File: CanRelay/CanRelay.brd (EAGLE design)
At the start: 93 x 65.5 mm, 22 parts

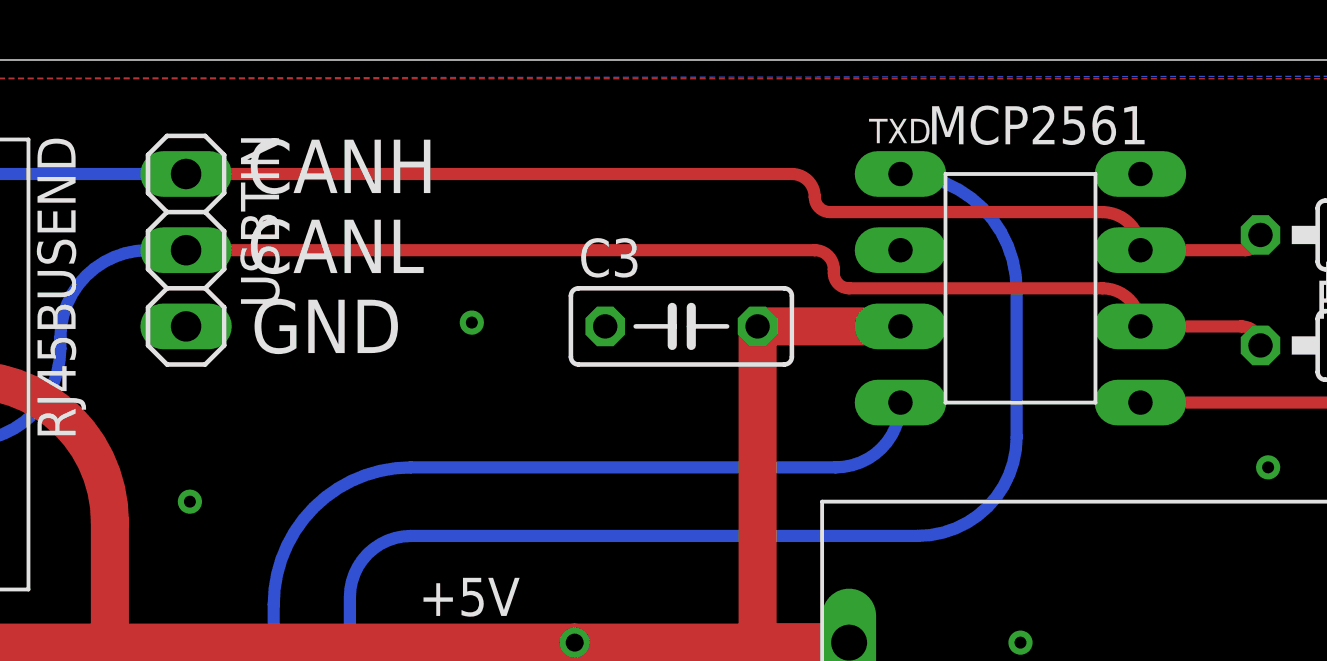
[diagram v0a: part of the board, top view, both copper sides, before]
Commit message: final tweaks on CanRelay - moving CANH and CANL lines around transceiver as opposed to among its pads. Moved therefore 5V for transceiver to bottom layer. final tweaks of isolation of both ground planes
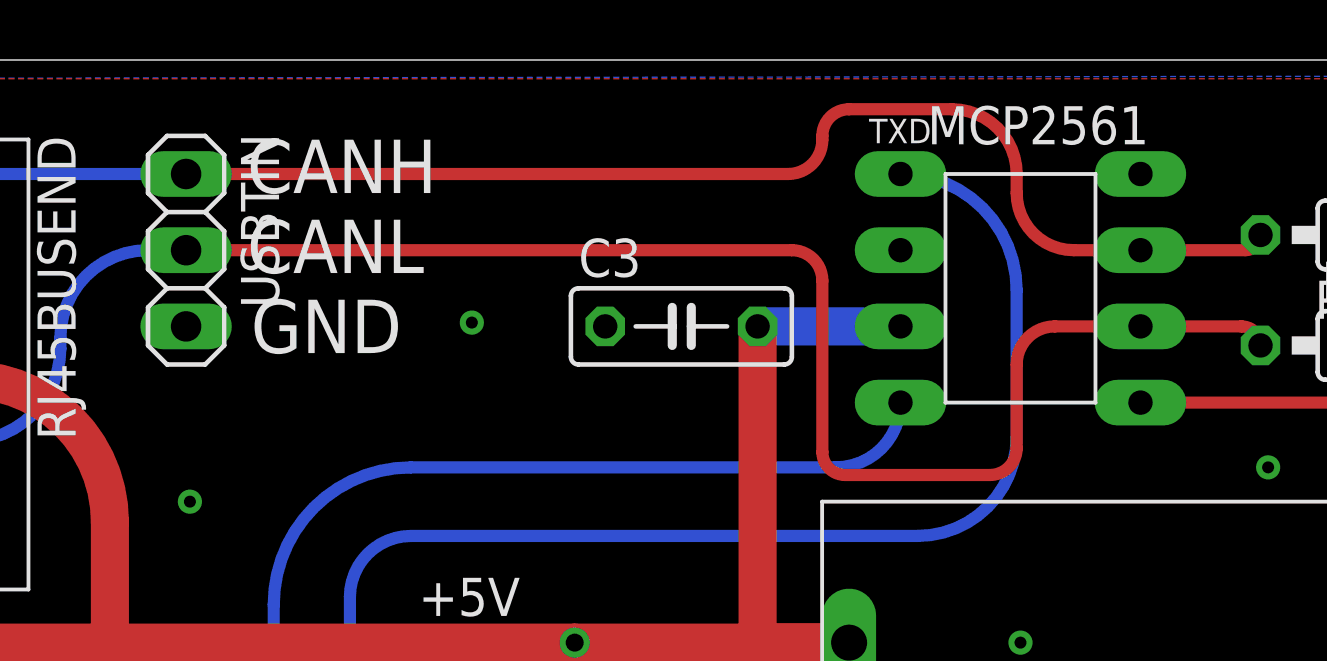
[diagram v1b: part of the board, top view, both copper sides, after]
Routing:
- net CANL: track 47.3 -> 56.3 mm
- net CANH: track 58.8 -> 61.0 mm
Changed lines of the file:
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@@
 <wire x1="13.808" y1="58.942" x2="13.808" y2="56.902" width="1.27" layer="1"/>
 <wire x1="13.808" y1="56.902" x2="13.808" y2="54.862" width="1.27" layer="1"/>
-<wire x1="44.895" y1="56.642" x2="40.132" y2="56.642" width="1.27" layer="1"/>
 <wire x1="5.461" y1="32.385" x2="8.763" y2="35.687" width="1.27" layer="1" curve="90"/>
 <wire x1="8.763" y1="35.687" x2="8.763" y2="42.672" width="1.27" layer="1"/>
@@
 <wire x1="34.163" y1="35.941" x2="34.036" y2="46.101" width="1.27" layer="16" curve="1.43232"/>
 <via x="34.036" y="46.101" extent="1-16" drill="0.6"/>
+<wire x1="40.132" y1="56.642" x2="44.895" y2="56.642" width="1.27" layer="16"/>
 </signal>
 <signal name="GND">
@@
 <contactref element="PWR" pad="GND1"/>
 <contactref element="PWR" pad="GND2"/>
-<polygon width="0.4064" layer="1" isolate="1">
+<polygon width="0.4064" layer="1" isolate="0.89">
 <vertex x="0.762" y="64.897"/>
 <vertex x="92.5" y="64.897"/>
@@
 </polygon>
 <contactref element="USBTIN" pad="3"/>
-<polygon width="0.4064" layer="16" isolate="1">
+<polygon width="0.4064" layer="16" isolate="0.6">
 <vertex x="0.762" y="64.897"/>
 <vertex x="92.5" y="65.024"/>
@@
 <wire x1="56.388" y1="59.182" x2="52.895" y2="59.182" width="0.4064" layer="1"/>
 <contactref element="USBTIN" pad="1"/>
-<wire x1="21.082" y1="61.722" x2="41.275" y2="61.722" width="0.4064" layer="1"/>
-<wire x1="52.895" y1="59.182" x2="51.625" y2="60.452" width="0.4064" layer="1" curve="90"/>
-<wire x1="51.625" y1="60.452" x2="42.545" y2="60.452" width="0.4064" layer="1"/>
-<wire x1="42.545" y1="60.452" x2="42.037" y2="60.96" width="0.4064" layer="1" curve="-90"/>
-<wire x1="42.037" y1="60.96" x2="41.275" y2="61.722" width="0.4064" layer="1" curve="90"/>
 <contactref element="RJ45BUSEND" pad="RJ45_8"/>
 <wire x1="11.268" y1="51.802" x2="8.89" y2="54.18" width="0.4064" layer="16" curve="-90"/>
@@
 <wire x1="8.89" y1="59.309" x2="11.303" y2="61.722" width="0.4064" layer="16" curve="-90"/>
 <wire x1="11.303" y1="61.722" x2="21.082" y2="61.722" width="0.4064" layer="16"/>
+<wire x1="21.082" y1="61.722" x2="41.148" y2="61.722" width="0.4064" layer="1"/>
+<wire x1="41.148" y1="61.722" x2="42.291" y2="62.865" width="0.4064" layer="1" curve="90"/>
+<wire x1="42.291" y1="62.865" x2="42.291" y2="62.992" width="0.4064" layer="1"/>
+<wire x1="42.291" y1="62.992" x2="43.18" y2="63.881" width="0.4064" layer="1" curve="-90"/>
+<wire x1="43.18" y1="63.881" x2="46.609" y2="63.881" width="0.4064" layer="1"/>
+<wire x1="46.609" y1="63.881" x2="48.768" y2="61.722" width="0.4064" layer="1" curve="-90"/>
+<wire x1="48.768" y1="61.722" x2="48.768" y2="61.087" width="0.4064" layer="1"/>
+<wire x1="48.768" y1="61.087" x2="50.673" y2="59.182" width="0.4064" layer="1" curve="90"/>
+<wire x1="50.673" y1="59.182" x2="52.895" y2="59.182" width="0.4064" layer="1"/>
 </signal>
 <signal name="CANL">
@@
 <wire x1="56.261" y1="56.642" x2="52.895" y2="56.642" width="0.4064" layer="1"/>
 <contactref element="USBTIN" pad="2"/>
-<wire x1="52.895" y1="56.642" x2="51.625" y2="57.912" width="0.4064" layer="1" curve="90"/>
-<wire x1="51.625" y1="57.912" x2="43.18" y2="57.912" width="0.4064" layer="1"/>
-<wire x1="21.082" y1="59.182" x2="42.037" y2="59.182" width="0.4064" layer="1"/>
-<wire x1="42.037" y1="59.182" x2="42.672" y2="58.547" width="0.4064" layer="1" curve="-90"/>
-<wire x1="42.672" y1="58.547" x2="42.672" y2="58.42" width="0.4064" layer="1"/>
-<wire x1="42.672" y1="58.42" x2="43.18" y2="57.912" width="0.4064" layer="1" curve="90"/>
 <contactref element="RJ45BUSEND" pad="RJ45_7"/>
 <wire x1="13.808" y1="52.822" x2="16.891" y2="55.905" width="0.4064" layer="16" curve="90"/>
@@
 <wire x1="16.891" y1="56.261" x2="19.812" y2="59.182" width="0.4064" layer="16" curve="-90"/>
 <wire x1="19.812" y1="59.182" x2="21.082" y2="59.182" width="0.4064" layer="16"/>
+<wire x1="21.082" y1="59.182" x2="41.275" y2="59.182" width="0.4064" layer="1"/>
+<wire x1="41.275" y1="59.182" x2="42.291" y2="58.166" width="0.4064" layer="1" curve="-90"/>
+<wire x1="42.291" y1="58.166" x2="42.291" y2="52.451" width="0.4064" layer="1"/>
+<wire x1="42.291" y1="52.451" x2="43.053" y2="51.689" width="0.4064" layer="1" curve="90"/>
+<wire x1="43.053" y1="51.689" x2="47.879" y2="51.689" width="0.4064" layer="1"/>
+<wire x1="47.879" y1="51.689" x2="48.768" y2="52.578" width="0.4064" layer="1" curve="90"/>
+<wire x1="48.768" y1="52.578" x2="48.768" y2="55.372" width="0.4064" layer="1"/>
+<wire x1="48.768" y1="55.372" x2="50.038" y2="56.642" width="0.4064" layer="1" curve="-90"/>
+<wire x1="50.038" y1="56.642" x2="52.895" y2="56.642" width="0.4064" layer="1"/>
 </signal>
 <signal name="TXD">

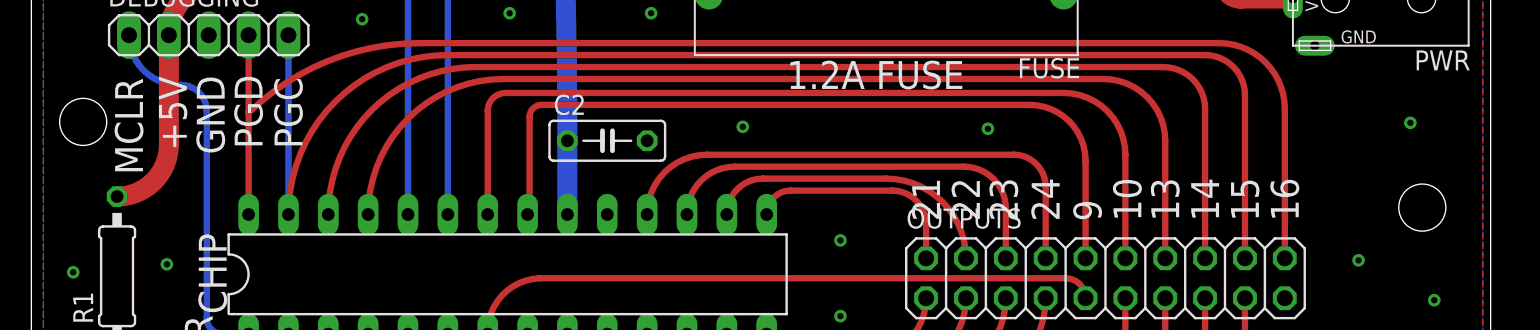
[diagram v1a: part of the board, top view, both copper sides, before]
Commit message: #17 replaced RJ45 for inputs with 5 PTR 2pins   - RJ45 dropped and up to 5 individual PTR inputs I already bought   added to the board so that they can be connected if needed   - has the advantage of simple board for just 1 switch - the same as   before, but I can really wire up all 8 inputs of a can switch now if   needed   - also better work with cables using this big inputs switch   - moved things around on the board, did not change dimension of the   board in the end   - moved double RJ45 a bit to the left   - rewired CAN lines, used thick line as well this time   - updated isolation for GND copper boards   - all wired up, perhaps just fine tune labels next time
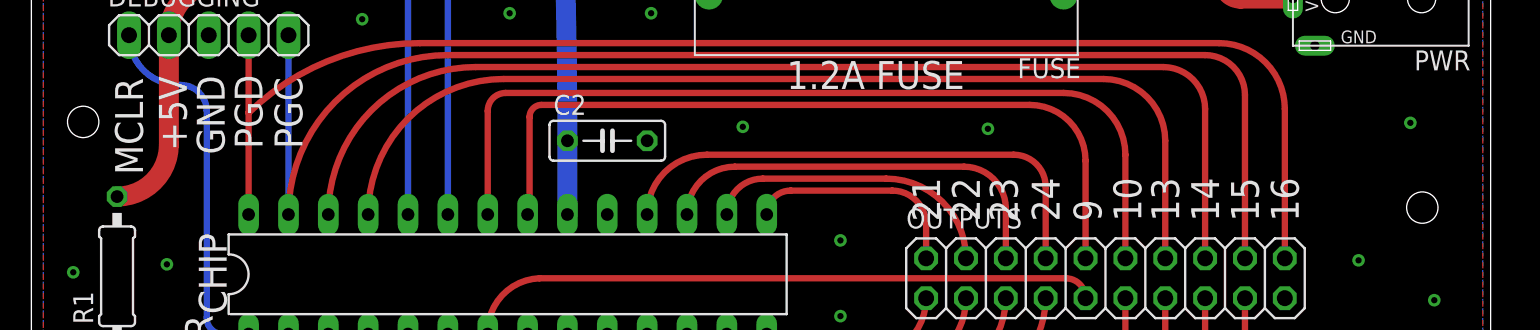
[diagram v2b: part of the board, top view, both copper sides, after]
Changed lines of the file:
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@@
 By Lubos Housa
 https://github.com/PoJD/can-pcb</text>
-<hole x="3.302" y="37.143" drill="3"/>
-<hole x="88.646" y="31.682" drill="3"/>
+<hole x="3.302" y="37.143" drill="2"/>
+<hole x="88.646" y="31.682" drill="2"/>
 <text x="23.114" y="61.087" size="1.778" layer="21">CANH</text>
 <text x="23.114" y="58.42" size="1.778" layer="21">CANL</text>

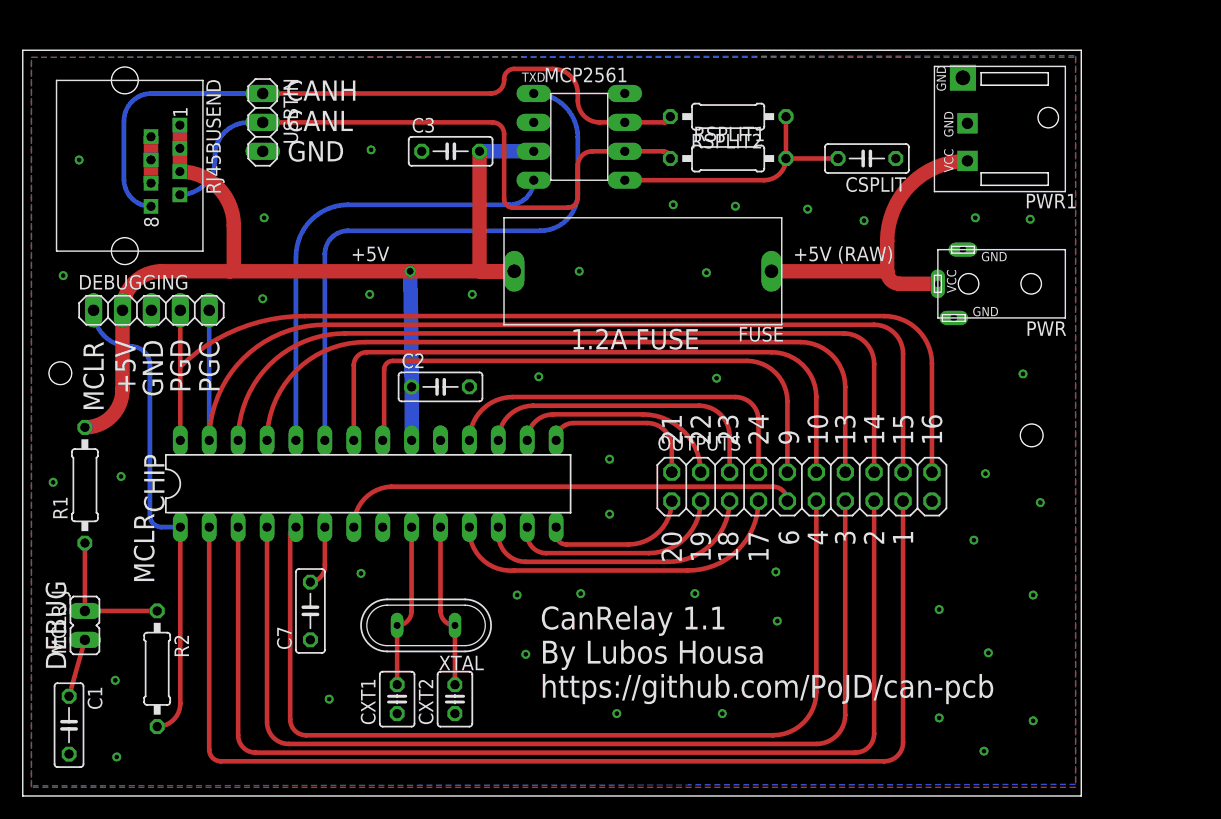
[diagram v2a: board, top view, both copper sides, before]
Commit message: #19 dropped old chip, put new chip from eagle library on the schematic. put all mandatory connections to the chip so far only, so one more capacitor since this variant has 2 pairs of VSS and VDD pins, put all to schema, including MCLR, voltage reg, input power, crystal pins. Schema is therefore done for all but outputs. Board half way through
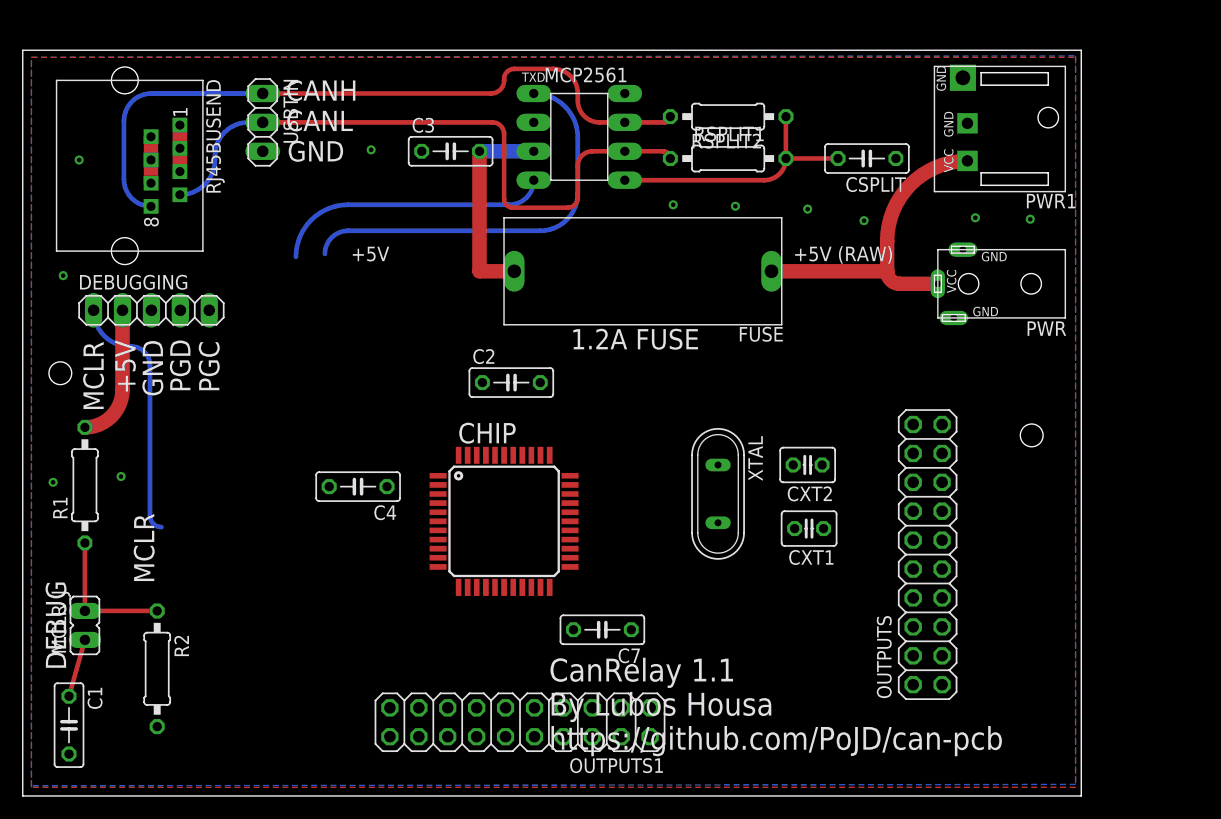
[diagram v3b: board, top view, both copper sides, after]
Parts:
- added C4: 0.1uF, rcl:C050-025X075
- added OUTPUTS1: (no value), pinhead:2X10
- CHIP: value PIC18F2480-I/SP -> PIC18F45K80_TQFPI/P; device microchip:DIL28-3 -> PoJD:TQFP44
- moved CXT1 39.2 mm to (69.1, 23.5), turned to 180 degrees
- moved CXT2 37.2 mm to (69.0, 29.1), turned to 180 degrees
- moved XTAL 28.1 mm to (61.1, 26.5), turned to 270 degrees
- moved C7 25.7 mm to (50.9, 14.6), turned to 180 degrees
- moved OUTPUTS 12.6 mm to (79.5, 21.2), turned to 90 degrees
- moved CHIP 12.4 mm to (42.3, 24.1)
- moved C2 6.23 mm to (42.9, 36.3)
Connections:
- net +5V: now also C4.1, CHIP.28, CHIP.7; no longer CHIP.20
- net GND: now also C4.2, CHIP.29, CHIP.6; no longer CHIP.19, CHIP.8
- net MCLR: now also CHIP.18; no longer CHIP.1
- net N$4: now also CHIP.23; no longer CHIP.6
- net O1: no longer CHIP.2
- net O10: no longer CHIP.22
- net O13: no longer CHIP.25
- net O14: no longer CHIP.26
- net O17: no longer CHIP.11
- net O18: no longer CHIP.12
- net O19: no longer CHIP.13
- net O2: no longer CHIP.3
- net O20: no longer CHIP.14
- net O21: no longer CHIP.15
- net O22: no longer CHIP.16
- net O23: no longer CHIP.17
- net O24: no longer CHIP.18
- net O3: no longer CHIP.4
- net O4: no longer CHIP.5
- net O6: no longer CHIP.7
- net O9: no longer CHIP.21
- net OSC1: now also CHIP.30; no longer CHIP.9
- net OSC2: now also CHIP.31; no longer CHIP.10
- net PGC/O15: no longer CHIP.27
- net PGD/O16: no longer CHIP.28
- net RXD: no longer CHIP.24
- net TXD: no longer CHIP.23
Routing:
- net O1: track 102.8 -> 0.00 mm
- net O2: track 95.9 -> 0.00 mm
- net PGD/O16: track 89.6 -> 0.00 mm
- net O3: track 88.6 -> 0.00 mm
- net PGC/O15: track 88.1 -> 0.00 mm
- net O4: track 82.3 -> 0.00 mm
- net O14: track 70.4 -> 0.00 mm
- net O13: track 63.5 -> 0.00 mm
- net +5V: track 96.6 -> 35.0 mm, vias 1 -> 0
- net O10: track 56.0 -> 0.00 mm
- net O9: track 49.7 -> 0.00 mm
- net O6: track 40.2 -> 0.00 mm
- net O24: track 32.4 -> 0.00 mm
- net O17: track 29.6 -> 0.00 mm
- net O23: track 25.9 -> 0.00 mm
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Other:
- board text removed: "1"
- board text removed: "10"
- board text removed: "13"
- board text removed: "14"
- board text removed: "15"
- board text removed: "16"
- board text removed: "17"
- board text removed: "18"
- board text removed: "19"
- board text removed: "2"
- board text removed: "20"
- board text removed: "21"
- board text removed: "22"
- board text removed: "23"
- board text removed: "24"
- board text removed: "3"
- board text removed: "4"
- board text removed: "6"
- board text removed: "9"
